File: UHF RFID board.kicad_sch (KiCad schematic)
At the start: 24 parts, among them J1 FZ_full_module, J10 SIM_Card, J11 SIM_Card, J2 picoblade, J4 Conn_02x03_Odd_Even, J5 Conn_02x04_Odd_Even, U1 YRM1001, U2 SEC1210

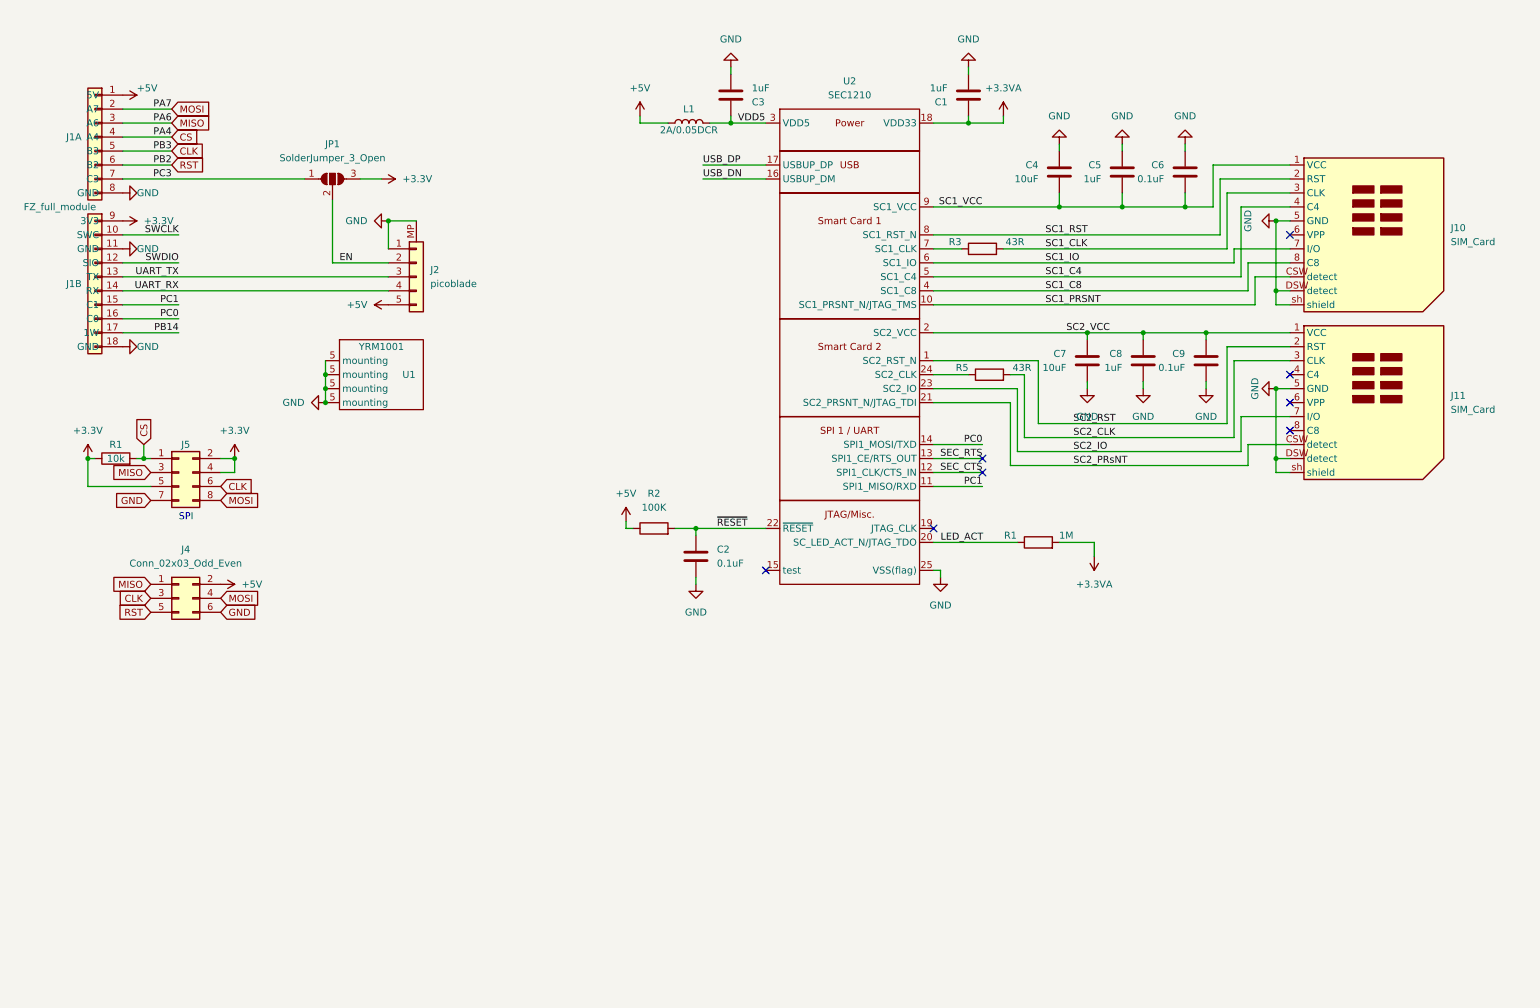
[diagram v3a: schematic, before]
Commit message: Update V2.1
- modified schematic to add iClass SE processor chip connections and symbol
- added footprints to enable direct mounting of iClass SE processor chips instead of using a SAM (https://www.hidglobal.com/products/sio-processor)
- added e.e.
- routing
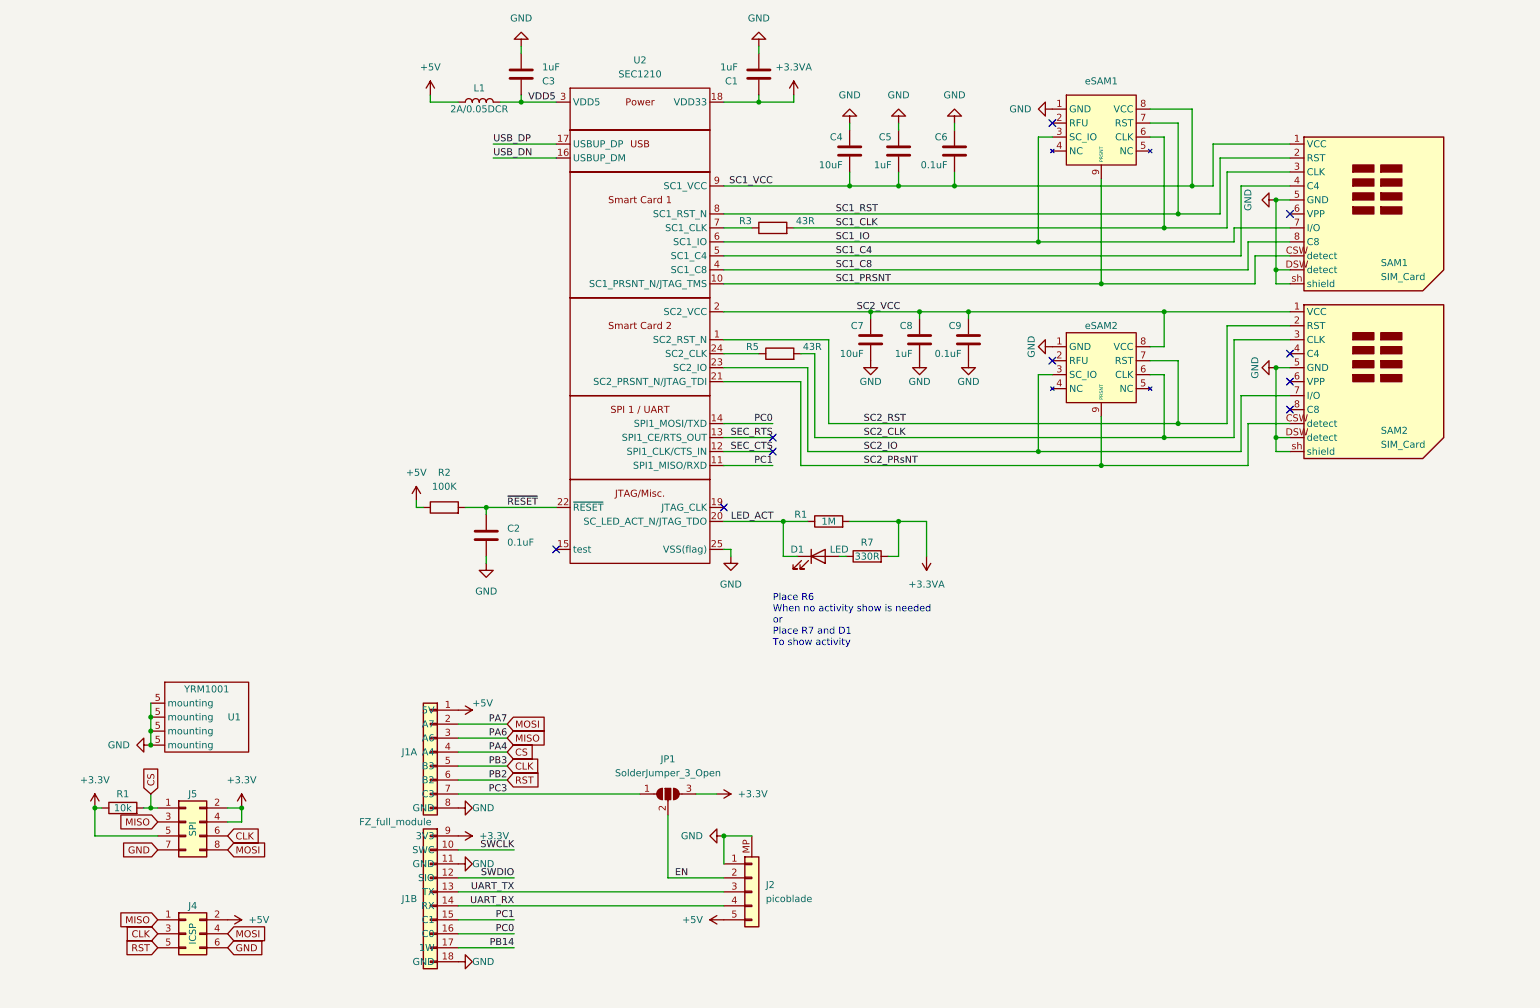
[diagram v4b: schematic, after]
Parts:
- added D1: LED, Custom LEDs:side-edge mount, symbol Device:LED
- added R7: 330R, Resistor_SMD:R_0402_1005Metric, symbol Device:R
- added eSAM1, eSAM2: ~, Package_DFN_QFN:DFN-8-1EP_5x5mm_P1.27mm_EP2.5x4mm, symbol custom symbols:HID_iCLASS_SE_Processor_-_SE3100A00
- J4: value Conn_02x03_Odd_Even -> ICSP
- J5: value Conn_02x04_Odd_Even -> SPI
- renumbered J10 to SAM1, J11 to SAM2
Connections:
- net +3.3VA: now also R7.2
- net GND: now also eSAM1.1 (GND), eSAM2.1 (GND)
- net LED_ACT: now also D1.1 (K)
- net SC1_CLK: now also eSAM1.6 (CLK)
- net SC1_IO: now also eSAM1.3 (SC_IO)
- net SC1_PRSNT: now also eSAM1.9 (PRSNT)
- net SC1_RST: now also eSAM1.7 (RST)
- net SC1_VCC: now also eSAM1.8 (VCC)
- net SC2_CLK: now also eSAM2.6 (CLK)
- net SC2_IO: now also eSAM2.3 (SC_IO)
- net SC2_PRsNT: now also eSAM2.9 (PRSNT)
- net SC2_RST: now also eSAM2.7 (RST)
- net SC2_VCC: now also eSAM2.8 (VCC)
- new net: D1.2 (A), R7.1
- no-connect marks 8 -> 10
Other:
- note added: "Place R6 When no activity show is needed or Place R7 and D1 To show activity"
- note removed: "SPI"
- moved on the sheet: C1, C2, C3, C4, C5, C6, C7, C8, C9, J1A, J1B, J2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

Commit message: fixes + bom, end of work on V2
Fixed some footprint directory inconsistencies and errors dating form at least the start of the SAM integration phase for some, Cleaned up / reworked some footprints and finalized others.
Fixed some BOM links being incorrect and/or missing.

That concludes work on V2. Next additions will go towards V3 if there ever is one, but the board is now getting very cramped, and will be in a branch now that I know how those work.
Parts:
- D1: mouser (none) -> https://www.mouser.fr/ProductDetail/604-APA1606VRBXF5MAV; spec (none) -> 1.6mm x 0.6mm side-view LED
- J4: mouser (none) -> https://www.mouser.fr/ProductDetail/Harwin/M20-9950345?qs=%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
- R1: mouser https://www.mouser.fr/ProductDetail/Bourns/CR0402-FX-3300GL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 -> (none); now not fitted
- R3: mouser https://www.mouser.fr/ProductDetail/652-CR0402FX-43R0GLF -> https://www.mouser.fr/ProductDetail/?qs=ePR1ZvdkOKKmGsQnUAr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
- R5: mouser (none) -> https://www.mouser.fr/ProductDetail/?qs=ePR1ZvdkOKKmGsQnUAr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
- R7: mouser (none) -> https://www.mouser.fr/ProductDetail/Bourns/CR0402-FX-3300GL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
- SAM1, SAM2: footprint Custom footprints:SIMMP-00801B000-G sim card connector -> Custom footprints:SIMMP-00801B000-G sim card connector w plated holes; symbol nard_sam:SIM_Card -> custom symbols:SIM_Card_slot; farnell https://fr.farnell.com/multicomp/simmp-00601b000-g/connecte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 -> https://fr.farnell.com/multicomp/simmp-00801b000-g/connecte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
- eSAM1, eSAM2: footprint Package_DFN_QFN:DFN-8-1EP_5x5mm_P1.27mm_EP2.5x4mm -> Custom footprints:DFN-8-splitEP_5x5mm_P1.27mm_EP2.5x4mm; now not fitted; now left out of the parts list
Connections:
- net GND: no longer SAM1.sh (shield), SAM2.sh (shield), U1.2 (status/to_NUC_ICE-DAT), U1.3 (to_NUC_ICE-CLK), U1.4 (to_NUC_nRST)
- no-connect marks 10 -> 14

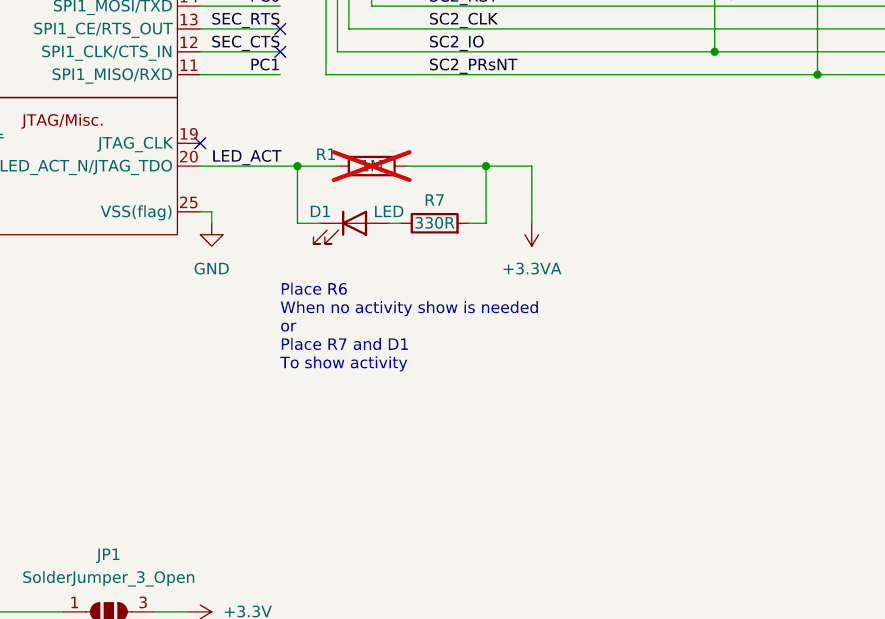
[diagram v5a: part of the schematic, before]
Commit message: V2.3 release
Switched a resistor and capacitor to B.cu to ensure they don't get ripped off when removing the picoblade connector. depending on further testing to see if I can get the LEDout working on the SEC chip, might do the same with R1 and remove D1 and D2 and the associated resistor. 
Cleaned up routing a bit due to that change.
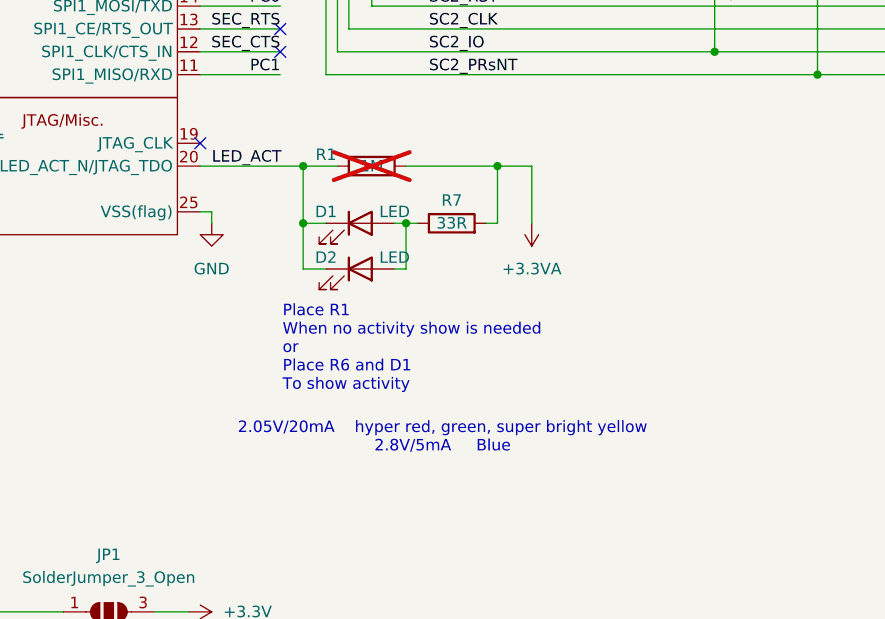
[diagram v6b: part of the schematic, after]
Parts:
- added D2: LED, Custom LEDs:kingbright AGPA1602 - FLIPPED, symbol Device:LED
- D1: footprint Custom LEDs:side-edge mount -> Custom LEDs:kingbright AGPA1602
- R7: value 330R -> 33R; JLCPCB Part # C427206 -> (none); mouser https://www.mouser.fr/ProductDetail/Bourns/CR0402-FX-3300GL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 -> (none); spec 330R 5% -> 33R 5%
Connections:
- net LED_ACT: now also D2.1 (K)
- net at D1.2 (A), R7.1: now also D2.2 (A)
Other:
- note added: "2.05V/20mA hyper red, green, super bright yellow 2.8V/5mA Blue"
- note added: "Place R1 When no activity show is needed or Place R6 and D1 To show activity"
- note removed: "Place R6 When no activity show is needed or Place R7 and D1 To show activity"
- moved on the sheet: D1, R7

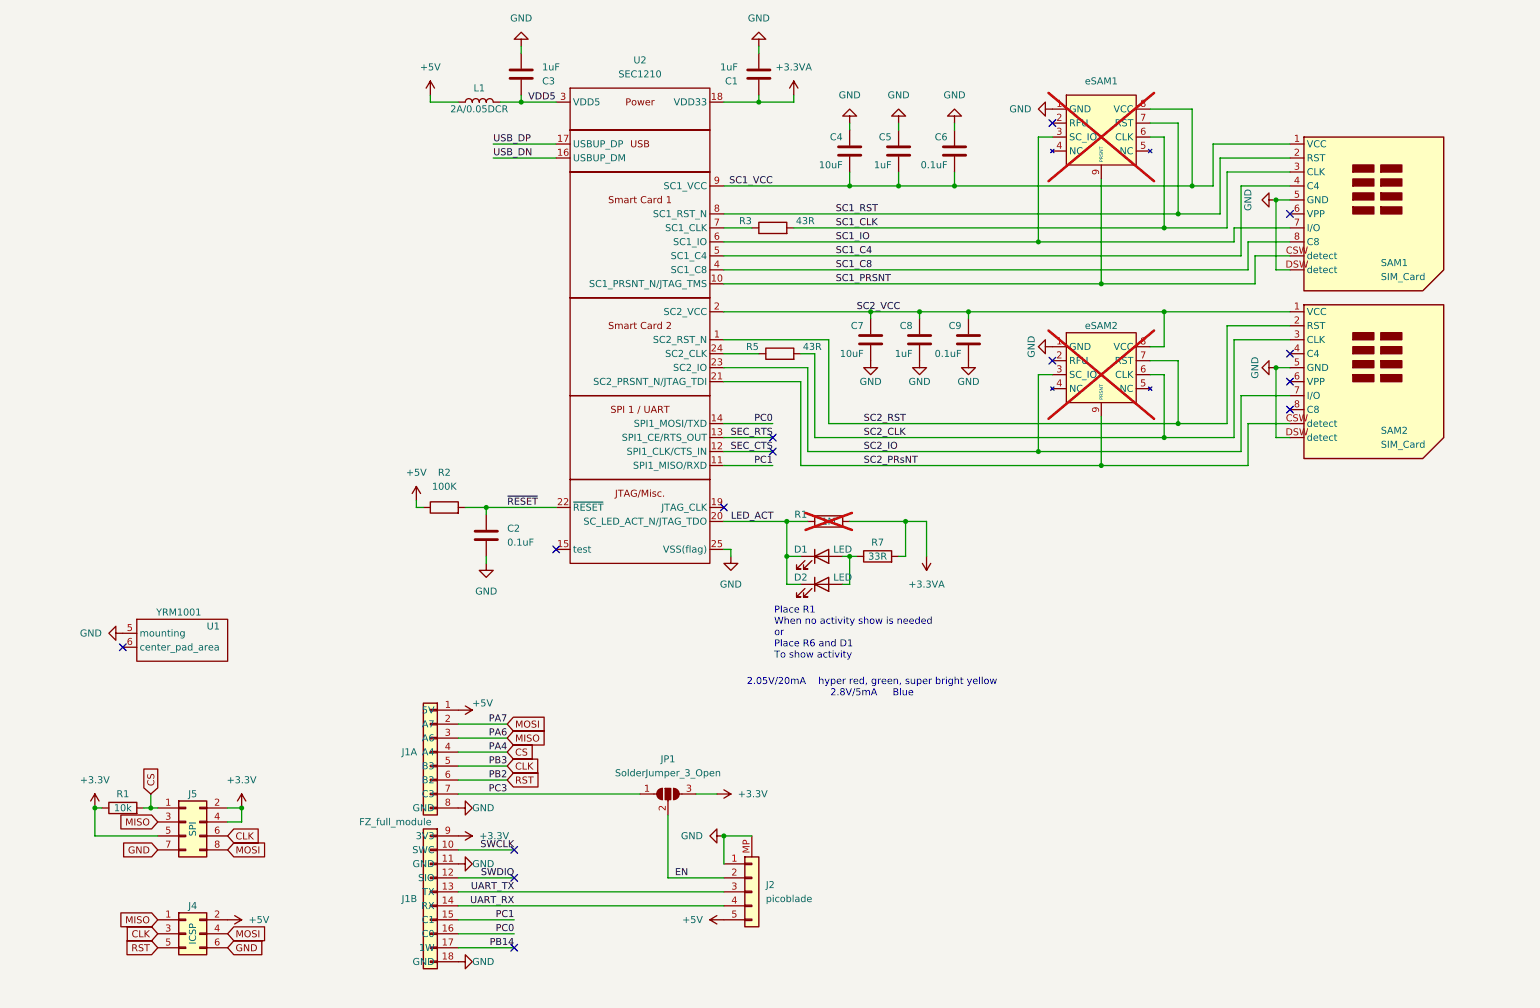
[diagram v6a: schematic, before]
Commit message: removed no longer needed features (LEDs, USB)
After testing it turns out the USB port on the SEC1210 UART version does not seem to be enabled. Therefore there's no way to program the chip to enable the LED output.
Removed unneeded D1, D2, R6, and re-positioned R1 and C1 thanks to the extra space.
updated schematic with DNP tags for D1, D2, R6.
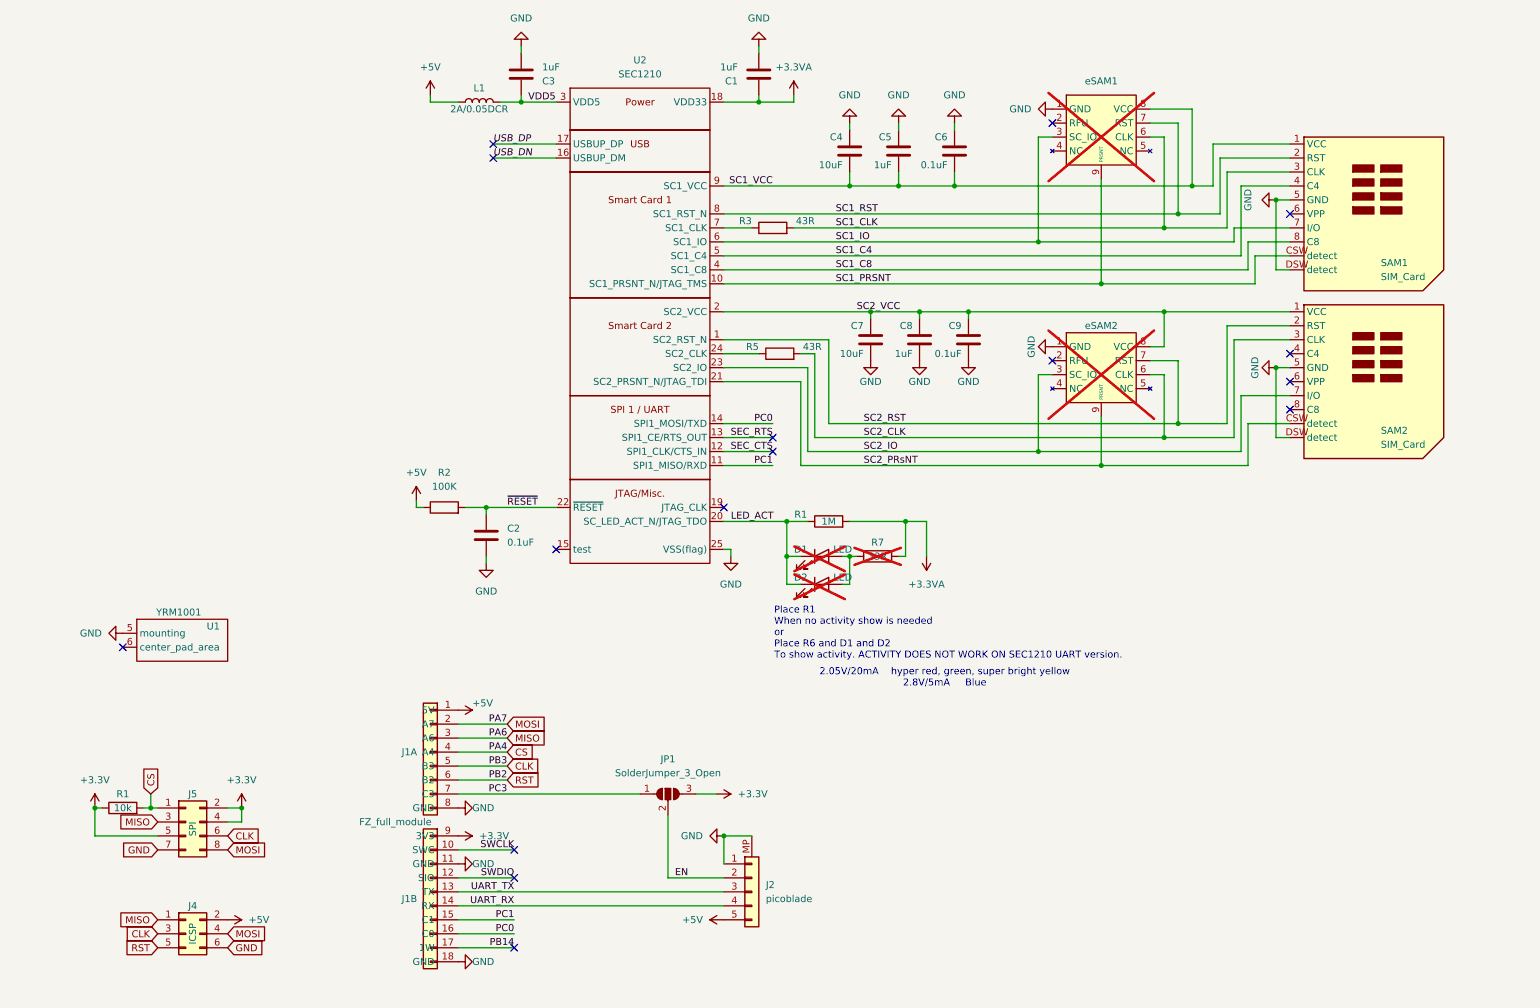
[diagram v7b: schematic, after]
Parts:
- D1, D2, R7: now not fitted
- R1: now fitted; now in the parts list
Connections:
- no-connect marks 14 -> 16
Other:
- note added: "Place R1 When no activity show is needed or Place R6 and D1 and D2 To show activity. ACTIVITY DOES NOT WORK ON SEC1210 UART version."
- note removed: "Place R1 When no activity show is needed or Place R6 and D1 To show activity"
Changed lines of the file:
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@@
 	)
 	(no_connect
+		(at 93.98 39.37)
+	)
+	(no_connect
 		(at 195.58 78.74)
 	)
@@
 	)
 	(no_connect
+		(at 93.98 41.91)
+	)
+	(no_connect
 		(at 105.41 113.03)
 	)
@@
 		)
 	)
-	(text "Place R1\nWhen no activity show is needed\nor\nPlace R6 and D1\nTo show activity"
+	(text "Place R1\nWhen no activity show is needed\nor\nPlace R6 and D1 and D2\nTo show activity. ACTIVITY DOES NOT WORK ON SEC1210 UART version."
 		(exclude_from_sim no)
 		(at 145.034 133.096 0)
@@
 	(text "2.05V/20mA	hyper red, green, super bright yellow\n2.8V/5mA 	Blue"
 		(exclude_from_sim no)
-		(at 162.814 138.176 0)
+		(at 176.022 136.398 0)
 		(effects
 			(font
@@
 			(font
 				(size 1.27 1.27)
+				(italic yes)
 			)
 			(justify left bottom)
@@
 			(font
 				(size 1.27 1.27)
+				(italic yes)
 			)
 			(justify left bottom)
@@
 		(exclude_from_sim no)
 		(in_bom no)
-		(on_board yes)
-		(dnp no)
+		(on_board no)
+		(dnp yes)
 		(property "Reference" "D2"
 			(at 149.86 118.11 0)
@@
 		(unit 1)
 		(exclude_from_sim no)
-		(in_bom no)
+		(in_bom yes)
 		(on_board yes)
-		(dnp yes)
+		(dnp no)
 		(property "Reference" "R1"
 			(at 149.86 106.68 90)
@@
 		(exclude_from_sim no)
 		(in_bom no)
-		(on_board yes)
-		(dnp no)
+		(on_board no)
+		(dnp yes)
 		(property "Reference" "D1"
 			(at 149.86 113.03 0)
@@
 		(exclude_from_sim no)
 		(in_bom no)
-		(on_board yes)
-		(dnp no)
+		(on_board no)
+		(dnp yes)
 		(property "Reference" "R7"
 			(at 163.83 111.76 90)
